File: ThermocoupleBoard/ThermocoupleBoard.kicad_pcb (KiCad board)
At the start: 4 copper layers, 62.6 x 50.4 mm, 62 parts, among them J2 1935161, J3 1935161, J4 1935161, J5 Conn_01x20_Pin, U1 LT1962-3.3, U2 MAX31856, U3 MAX31856, U4 MAX31856

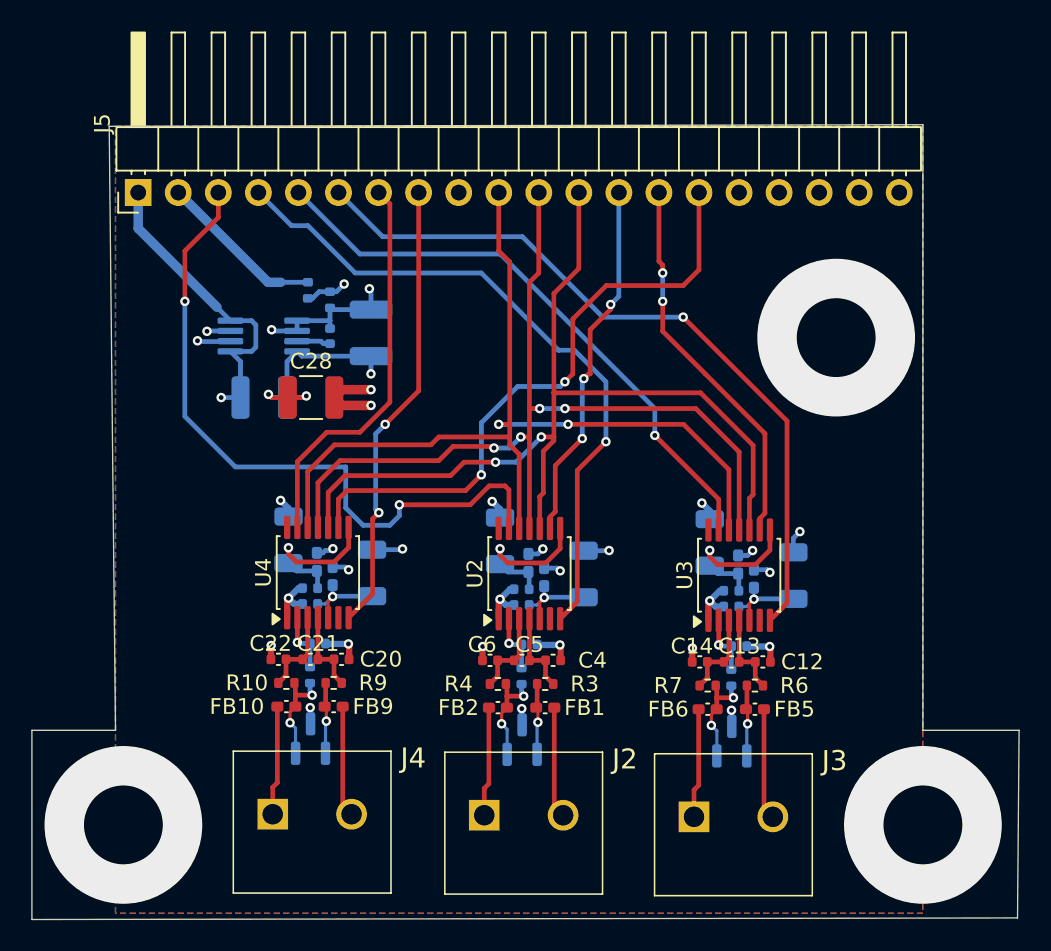
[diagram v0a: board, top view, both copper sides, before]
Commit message: add a unit test fixture, and start changing the current measurement circuit
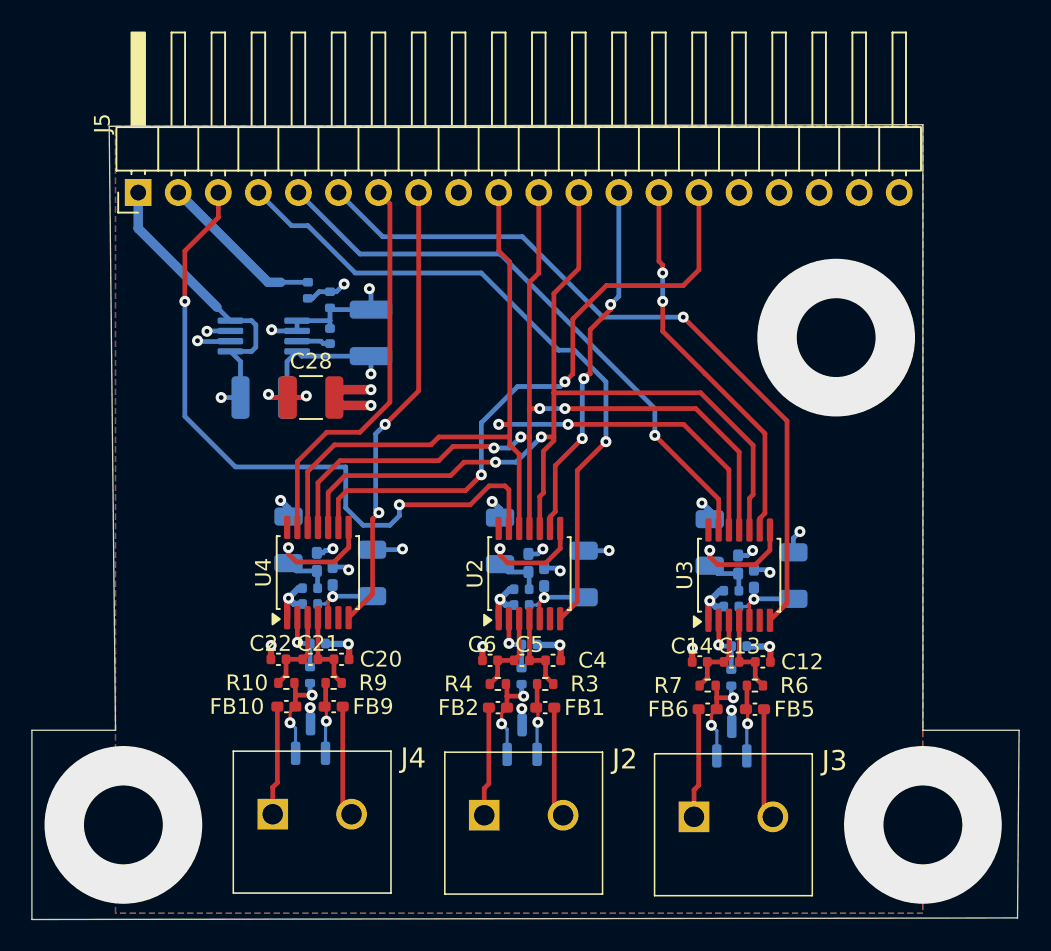
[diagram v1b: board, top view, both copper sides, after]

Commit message: final pcb?
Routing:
- net GND: track 46.4 -> 67.6 mm, vias 21 -> 52
- net Net-(U2-BIAS): track 3.91 -> 8.83 mm
- net Net-(U4-BIAS): track 3.91 -> 8.19 mm
- net Net-(U4-DVDD): track 10.2 -> 13.5 mm
- net Net-(U2-DVDD): track 10.2 -> 12.5 mm
- net Net-(U3-DVDD): track 10.2 -> 12.2 mm
- net Net-(U3-AVDD): track 5.84 -> 7.69 mm
- net 3.3_D: track 57.5 -> 55.9 mm
- net 3.3V_A: track 59.4 -> 60.8 mm
- net /thermoDrdy_1: track 47.5 -> 48.4 mm
- net unconnected-(U1-NC-Pad7): track 1.50 -> 2.12 mm
- added copper zone on In2.Cu, net GND
